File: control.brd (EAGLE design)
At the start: 100 x 20 mm, 0 parts

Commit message: adds H-bridge
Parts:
- added U$1: CHIP_PRO, CHIP_Pro-Footprint:CHIP_PRO
- added U1, U4: AL5802-7, LED Driver:SOT26
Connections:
- new net 24V: U1.2, U4.2
- new net CHG-IN: U$1.CHG-IN
- new net GND: U$1.AGND, U$1.GND@0, U$1.GND@1, U$1.GND@2, U$1.GND@3, U$1.GND@4, U$1.GND@6, U$1.GND@7, U1.4
- new net IPSOUT: U$1.IPSOUT
- new net N$1: U1.1
- new net N$2: U4.5, U4.6
- new net N$3: U1.5, U1.6
- new net N$4: U4.4
- new net N$5: U1.3
- new net N$7: U4.3
- new net N$8: U4.1
- new net VBUS: U$1.VBUS
- new net VCC3V3: U$1.VCC3V3
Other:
- board size 100 x 20 mm -> 883.9 x 101.3 mm

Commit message: adds LED driver
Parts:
- removed U1, U4: AL5802-7, LED Driver:SOT26
- added C1: UVR0J102MPD1TA, Smile_Shade:U1-M
- added C2: ESK107M025AE3EA, Smile_Shade:E-E3
- added R1, R10, R11, R12, R13, R14, R15, R16, R2, R3, R4, R5, R6, R7, R8, R9: RC0603FR-0710RL, LED Driver:RC0603N
- added U$10, U$12, U$14, U$16, U$18, U$20, U$22, U$24, U$26, U$28, U$30, U$32, U$34, U$4, U$6, U$8: 2N7002P, LED Driver:SOT23
- added U$11, U$13, U$15, U$17, U$19, U$21, U$23, U$25, U$27, U$29, U$3, U$31, U$33, U$5, U$7, U$9: NUD4011DR2G, LED Driver:8SOIC
- added U$2: L293DNE, LED Driver:NE16
- added U$35: LM2576HVT-5.0/NOPB, LED Driver:T05A
- added U$36: SRN8040-101M, Smile_Shade:IND_BOURNS_SRN8040
- moved U$1 55.0 mm to (25.4, 17.8), turned to 90 degrees
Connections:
- removed net CHG-IN: U$1.CHG-IN
- new net 48V: C2.1, R1.2, R10.2, R11.2, R12.2, R13.2, R14.2, R15.2, R16.2, R2.2, R3.2, R4.2, R5.2, R6.2, R7.2, R8.2, R9.2, U$11.P$1, U$13.P$1, U$15.P$1, U$17.P$1, U$19.P$1, U$21.P$1, U$23.P$1, U$25.P$1, U$27.P$1, U$29.P$1, U$3.P$1, U$31.P$1, U$33.P$1, U$5.P$1, U$7.P$1, U$9.P$1
- new net 5V: C1.2, U$1.CHG-IN, U$2.16, U$35.4, U$36.2
- new net AGND: U$1.AGND
- new net DIR1A: U$2.7
- new net LEDSTR_1: U$17.P$5, U$17.P$6, U$17.P$7, U$17.P$8
- new net LEDSTR_10: U$21.P$5, U$21.P$6, U$21.P$7, U$21.P$8
- new net LEDSTR_11: U$23.P$5, U$23.P$6, U$23.P$7, U$23.P$8
- new net LEDSTR_12: U$25.P$5, U$25.P$6, U$25.P$7, U$25.P$8
- new net LEDSTR_13: U$27.P$5, U$27.P$6, U$27.P$7, U$27.P$8
- new net LEDSTR_14: U$29.P$5, U$29.P$6, U$29.P$7, U$29.P$8
- new net LEDSTR_15: U$31.P$5, U$31.P$6, U$31.P$7, U$31.P$8
- new net LEDSTR_16: U$33.P$5, U$33.P$6, U$33.P$7, U$33.P$8
- new net LEDSTR_2: U$3.P$5, U$3.P$6, U$3.P$7, U$3.P$8
- new net LEDSTR_3: U$5.P$5, U$5.P$6, U$5.P$7, U$5.P$8
- new net LEDSTR_4: U$7.P$5, U$7.P$6, U$7.P$7, U$7.P$8
- new net LEDSTR_5: U$9.P$5, U$9.P$6, U$9.P$7, U$9.P$8
- new net LEDSTR_6: U$11.P$5, U$11.P$6, U$11.P$7, U$11.P$8
- new net LEDSTR_7: U$13.P$5, U$13.P$6, U$13.P$7, U$13.P$8
- new net LEDSTR_8: U$15.P$5, U$15.P$6, U$15.P$7, U$15.P$8
- new net LEDSTR_9: U$19.P$5, U$19.P$6, U$19.P$7, U$19.P$8
- new net M1B: U$2.6
- new net M2A: U$2.14
- new net N$10: R5.1, U$11.P$3
- new net N$11: U$13.P$4, U$14.P$3
- new net N$12: R6.1, U$13.P$3
- new net N$13: U$15.P$4, U$16.P$3
- new net N$14: R7.1, U$15.P$3
- new net N$15: U$17.P$4, U$18.P$3
- new net N$16: R8.1, U$17.P$3
- new net N$17: U$19.P$4, U$20.P$3
- new net N$18: R9.1, U$19.P$3
- new net N$19: U$21.P$4, U$22.P$3
- new net N$20: R10.1, U$21.P$3
- new net N$21: U$23.P$4, U$24.P$3
- new net N$22: R11.1, U$23.P$3
- new net N$23: U$25.P$4, U$26.P$3
- new net N$24: R12.1, U$25.P$3
- new net N$25: U$27.P$4, U$28.P$3
- new net N$26: R13.1, U$27.P$3
- new net N$27: U$29.P$4, U$30.P$3
- new net N$28: R14.1, U$29.P$3
- new net N$29: U$31.P$4, U$32.P$3
- new net N$30: R15.1, U$31.P$3
- new net N$31: U$33.P$4, U$34.P$3
- new net N$32: R16.1, U$33.P$3
- new net N$33: U$35.2, U$36.1
- new net N$34: C2.2, U$35.1
- new net N$6: R3.1, U$7.P$3
- new net N$9: U$11.P$4, U$12.P$3
- new net PWMLED1: U$4.P$2
- new net PWMLED10: U$22.P$2
- new net PWMLED11: U$24.P$2
- new net PWMLED12: U$26.P$2
- new net PWMLED13: U$28.P$2
- new net PWMLED14: U$30.P$2
- new net PWMLED15: U$32.P$2
- new net PWMLED16: U$34.P$2
- new net PWMLED2: U$6.P$2
- new net PWMLED3: U$8.P$2
- new net PWMLED4: U$10.P$2
- new net PWMLED5: U$12.P$2
- new net PWMLED6: U$14.P$2
- new net PWMLED7: U$16.P$2
- new net PWMLED8: U$18.P$2
- new net PWMLED9: U$20.P$2
- net 24V: now also U$2.8; no longer U1.2, U4.2
- net GND: now also C1.1, U$10.P$1, U$12.P$1, U$14.P$1, U$16.P$1, U$18.P$1, U$2.12, U$2.13, U$2.4, U$2.5, U$20.P$1, U$22.P$1, U$24.P$1, U$26.P$1, U$28.P$1, U$30.P$1, U$32.P$1, U$34.P$1, U$35.3, U$35.5, U$4.P$1, U$6.P$1, U$8.P$1; no longer U$1.AGND, U1.4
- net N$1: now also U$3.P$4, U$4.P$3; no longer U1.1
- net N$2: now also R1.1, U$3.P$3; no longer U4.5, U4.6
- net N$3: now also U$5.P$4, U$6.P$3; no longer U1.5, U1.6
- net N$4: now also R2.1, U$5.P$3; no longer U4.4
- net N$5: now also U$7.P$4, U$8.P$3; no longer U1.3
- net N$7: now also U$10.P$3, U$9.P$4; no longer U4.3
- net N$8: now also R4.1, U$9.P$3; no longer U4.1
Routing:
- net GND: track 0.00 -> 262.7 mm, vias 0 -> 4
- net 48V: track 0.00 -> 194.3 mm
- net 5V: track 0.00 -> 129.2 mm, vias 0 -> 1
- net N$33: track 0.00 -> 12.0 mm
- net N$34: track 0.00 -> 9.69 mm
- net N$19: track 0.00 -> 7.95 mm, vias 0 -> 1
- net N$25: track 0.00 -> 7.91 mm, vias 0 -> 1
- net N$15: track 0.00 -> 7.84 mm, vias 0 -> 1
- net N$11: track 0.00 -> 7.81 mm, vias 0 -> 1
- net N$21: track 0.00 -> 7.78 mm, vias 0 -> 1
- net N$5: track 0.00 -> 7.64 mm, vias 0 -> 1
- net N$13: track 0.00 -> 7.61 mm, vias 0 -> 1
- net N$23: track 0.00 -> 7.59 mm, vias 0 -> 1
- net N$31: track 0.00 -> 7.56 mm, vias 0 -> 1
- net N$3: track 0.00 -> 7.47 mm, vias 0 -> 1
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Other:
- board size 883.9 x 101.3 mm -> 172.7 x 35 mm

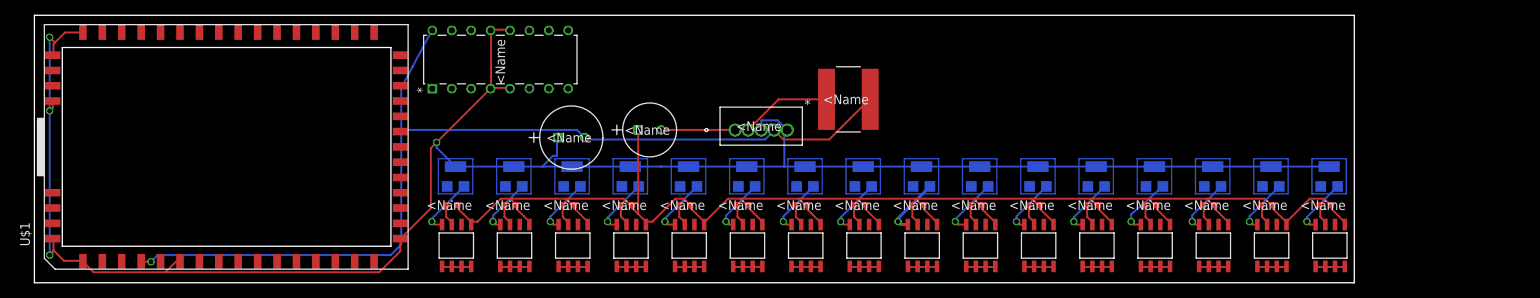
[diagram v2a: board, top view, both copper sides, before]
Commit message: adds PWM
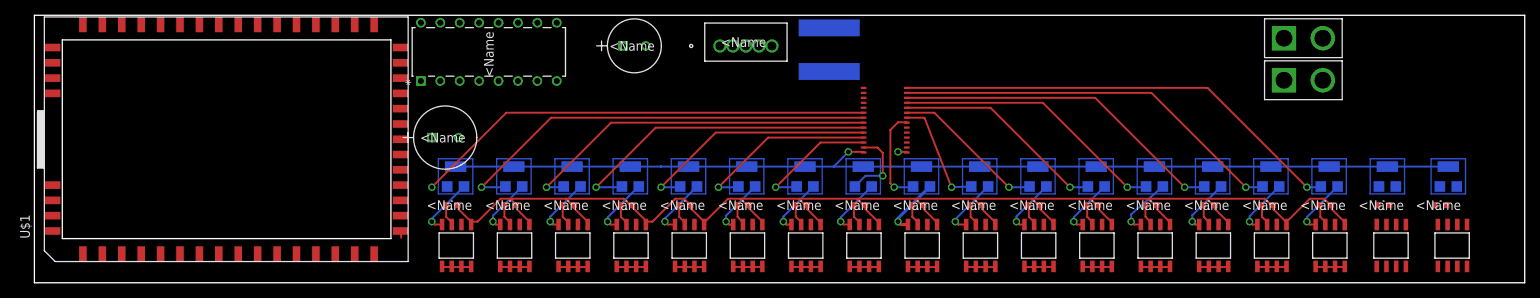
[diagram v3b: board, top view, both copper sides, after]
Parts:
- added R17, R18: RC0603FR-0710RL, LED Driver:RC0603N
- added U$37: PCA9685PW/Q900, Smile_Shade:SOT361-1
- added U$38, U$39: MOTORCONNECTOR, Smile_Shade:MOTORCONNECTOR
- added U$40, U$42: NUD4011DR2G, LED Driver:8SOIC
- added U$41, U$43: 2N7002P, LED Driver:SOT23
- moved C1 16.5 mm to (55.5, 19.0)
- moved C2 11.2 mm to (80.0, 31.0)
- moved U$35 11.2 mm to (96.5, 32.0)
- moved U$36 6.96 mm to (104.0, 30.5), flipped to the bottom, turned to 270 degrees
- moved U$2 1.80 mm to (68.3, 34.0)
- moved U$1 1.00 mm to (25.4, 18.8)
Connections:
- removed net PWMLED1: U$4.P$2
- removed net PWMLED10: U$22.P$2
- removed net PWMLED11: U$24.P$2
- removed net PWMLED12: U$26.P$2
- removed net PWMLED13: U$28.P$2
- removed net PWMLED14: U$30.P$2
- removed net PWMLED15: U$32.P$2
- removed net PWMLED16: U$34.P$2
- removed net PWMLED2: U$6.P$2
- removed net PWMLED3: U$8.P$2
- removed net PWMLED4: U$10.P$2
- removed net PWMLED5: U$12.P$2
- removed net PWMLED6: U$14.P$2
- removed net PWMLED7: U$16.P$2
- removed net PWMLED8: U$18.P$2
- removed net PWMLED9: U$20.P$2
- new net 48: R17.2, U$40.P$1
- new net LEDSTR_17: U$40.P$5, U$40.P$6, U$40.P$7, U$40.P$8
- new net LEDSTR_18: U$42.P$5, U$42.P$6, U$42.P$7, U$42.P$8
- new net M0: U$1.PWM0, U$2.1
- new net M1: U$1.PWM1, U$2.9
- new net M1A: U$2.3, U$38.P$2
- new net M2B: U$2.11, U$39.P$2
- new net N$35: U$40.P$4, U$41.P$3
- new net N$36: R17.1, U$40.P$3
- new net N$37: U$42.P$4, U$43.P$3
- new net N$38: R18.1, U$42.P$3
- new net SCK: U$1.TWI1-SCK, U$37.P$26
- new net SDA: U$1.TWI1-SDA, U$37.P$27
- new net ZN0: U$18.P$2, U$37.P$6
- new net ZN1: U$37.P$7, U$4.P$2
- new net ZN10: U$30.P$2, U$37.P$17
- new net ZN11: U$28.P$2, U$37.P$18
- new net ZN12: U$26.P$2, U$37.P$19
- new net ZN13: U$20.P$2, U$37.P$20
- new net ZN14: U$22.P$2, U$37.P$21
- new net ZN15: U$24.P$2, U$37.P$22
- new net ZN16: U$43.P$2
- new net ZN2: U$37.P$8, U$6.P$2
- new net ZN3: U$37.P$9, U$8.P$2
- new net ZN4: U$14.P$2, U$37.P$10
- new net ZN5: U$12.P$2, U$37.P$11
- new net ZN6: U$10.P$2, U$37.P$12
- new net ZN7: U$16.P$2, U$37.P$13
- new net ZN8: U$34.P$2, U$37.P$15, U$41.P$2
- new net ZN9: U$32.P$2, U$37.P$16
- net 48V: now also R18.2, U$42.P$1
- net 5V: now also U$37.P$28
- net GND: now also U$37.P$14, U$41.P$1, U$43.P$1
- net M1B: now also U$38.P$1
- net M2A: now also U$39.P$1
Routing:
- net 5V: track 129.2 -> 1.20 mm
- net GND: track 262.7 -> 135.7 mm, vias 4 -> 1
- net ZN0: track 0.00 -> 60.7 mm, vias 0 -> 1
- net ZN8: track 0.00 -> 59.6 mm, vias 0 -> 1
- net ZN1: track 0.00 -> 56.9 mm, vias 0 -> 1
- net ZN9: track 0.00 -> 51.7 mm, vias 0 -> 1
- net ZN2: track 0.00 -> 47.3 mm, vias 0 -> 1
- net ZN10: track 0.00 -> 43.8 mm, vias 0 -> 1
- net ZN3: track 0.00 -> 41.6 mm, vias 0 -> 1
- net ZN11: track 0.00 -> 35.9 mm, vias 0 -> 1
- net ZN4: track 0.00 -> 32.0 mm, vias 0 -> 1
- net ZN12: track 0.00 -> 28.0 mm, vias 0 -> 1
- net ZN5: track 0.00 -> 24.3 mm, vias 0 -> 1
- net ZN13: track 0.00 -> 20.1 mm, vias 0 -> 1
- net ZN6: track 0.00 -> 16.7 mm, vias 0 -> 1
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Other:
- board size 172.7 x 35 mm -> 195 x 35 mm

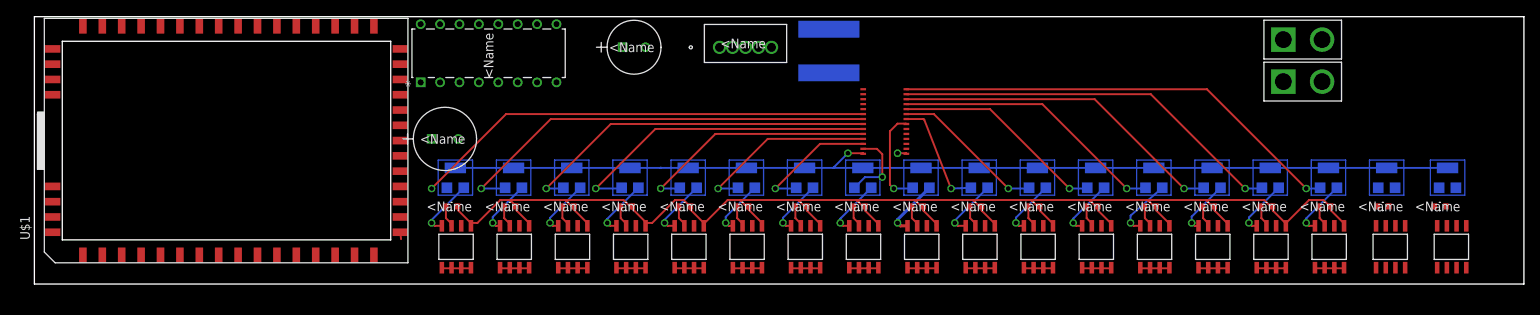
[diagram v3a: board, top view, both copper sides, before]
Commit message: adds flex connector
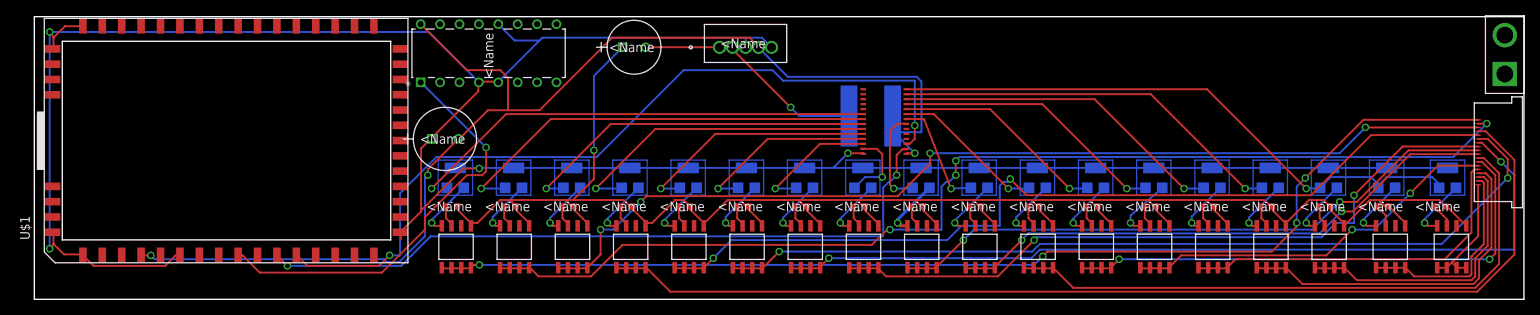
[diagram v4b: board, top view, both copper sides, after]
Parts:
- U$39: value MOTORCONNECTOR -> SFV18R-3STBE1HLF; device Smile_Shade:MOTORCONNECTOR -> Smile_Shade:SFV18R-3STBE1HLF
- moved U$39 31.8 mm to (189.0, 13.0), turned to 90 degrees
- moved U$38 29.0 mm to (192.5, 27.5), turned to 90 degrees
- moved U$36 10.1 mm to (109.5, 22.0), turned to 180 degrees
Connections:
- net LEDSTR_1: now also U$39.P$18
- net LEDSTR_10: now also U$39.P$9
- net LEDSTR_11: now also U$39.P$10
- net LEDSTR_12: now also U$39.P$7
- net LEDSTR_13: now also U$39.P$6
- net LEDSTR_14: now also U$39.P$5
- net LEDSTR_15: now also U$39.P$4
- net LEDSTR_16: now also U$39.P$3
- net LEDSTR_17: now also U$39.P$1
- net LEDSTR_18: now also U$39.P$2
- net LEDSTR_2: now also U$39.P$17
- net LEDSTR_3: now also U$39.P$16
- net LEDSTR_4: now also U$39.P$15
- net LEDSTR_5: now also U$39.P$12
- net LEDSTR_6: now also U$39.P$13
- net LEDSTR_7: now also U$39.P$14
- net LEDSTR_8: now also U$39.P$11
- net LEDSTR_9: now also U$39.P$8
- net M1A: no longer U$38.P$2
- net M1B: no longer U$38.P$1
- net M2A: now also U$38.P$1; no longer U$39.P$1
- net M2B: now also U$38.P$2; no longer U$39.P$2
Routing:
- net GND: track 135.7 -> 333.7 mm, vias 1 -> 4
- net 5V: track 1.20 -> 160.3 mm, vias 1 -> 3
- net LEDSTR_1: track 4.04 -> 147.0 mm, vias 0 -> 4
- net LEDSTR_2: track 3.97 -> 143.6 mm, vias 0 -> 4
- net LEDSTR_4: track 4.01 -> 139.7 mm
- net LEDSTR_3: track 4.03 -> 131.0 mm, vias 0 -> 4
- net LEDSTR_7: track 4.03 -> 117.4 mm, vias 0 -> 2
- net LEDSTR_6: track 3.97 -> 113.9 mm, vias 0 -> 2
- net LEDSTR_5: track 4.04 -> 112.2 mm, vias 0 -> 2
- net SCK: track 0.00 -> 106.5 mm, vias 0 -> 2
- net SDA: track 0.00 -> 94.6 mm, vias 0 -> 2
- net LEDSTR_8: track 4.02 -> 92.2 mm, vias 0 -> 2
- net LEDSTR_11: track 4.02 -> 81.3 mm, vias 0 -> 2
- net LEDSTR_9: track 3.97 -> 80.2 mm
- net LEDSTR_10: track 4.04 -> 73.5 mm, vias 0 -> 2
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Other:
- board size 195 x 35 mm -> 195 x 37 mm

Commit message: Revert "adds flex connector"
This reverts commit c0465f8f5036756819879aef16fe9e16a98b933a.
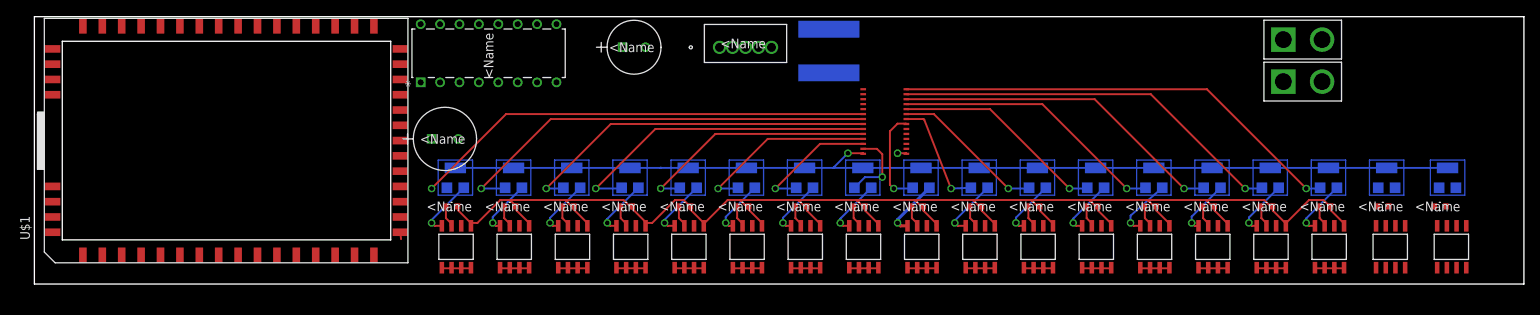
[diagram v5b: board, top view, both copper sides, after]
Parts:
- U$39: value SFV18R-3STBE1HLF -> MOTORCONNECTOR; device Smile_Shade:SFV18R-3STBE1HLF -> Smile_Shade:MOTORCONNECTOR
- moved U$39 31.8 mm to (163.5, 32.0), turned to 0 degrees
- moved U$38 29.0 mm to (163.5, 26.5), turned to 0 degrees
- moved U$36 10.1 mm to (104.0, 30.5), turned to 270 degrees
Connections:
- net LEDSTR_1: no longer U$39.P$18
- net LEDSTR_10: no longer U$39.P$9
- net LEDSTR_11: no longer U$39.P$10
- net LEDSTR_12: no longer U$39.P$7
- net LEDSTR_13: no longer U$39.P$6
- net LEDSTR_14: no longer U$39.P$5
- net LEDSTR_15: no longer U$39.P$4
- net LEDSTR_16: no longer U$39.P$3
- net LEDSTR_17: no longer U$39.P$1
- net LEDSTR_18: no longer U$39.P$2
- net LEDSTR_2: no longer U$39.P$17
- net LEDSTR_3: no longer U$39.P$16
- net LEDSTR_4: no longer U$39.P$15
- net LEDSTR_5: no longer U$39.P$12
- net LEDSTR_6: no longer U$39.P$13
- net LEDSTR_7: no longer U$39.P$14
- net LEDSTR_8: no longer U$39.P$11
- net LEDSTR_9: no longer U$39.P$8
- net M1A: now also U$38.P$2
- net M1B: now also U$38.P$1
- net M2A: now also U$39.P$1; no longer U$38.P$1
- net M2B: now also U$39.P$2; no longer U$38.P$2
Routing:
- net GND: track 333.7 -> 135.7 mm, vias 4 -> 1
- net 5V: track 160.3 -> 1.20 mm, vias 3 -> 1
- net LEDSTR_1: track 147.0 -> 4.04 mm, vias 4 -> 0
- net LEDSTR_2: track 143.6 -> 3.97 mm, vias 4 -> 0
- net LEDSTR_4: track 139.7 -> 4.01 mm
- net LEDSTR_3: track 131.0 -> 4.03 mm, vias 4 -> 0
- net LEDSTR_7: track 117.4 -> 4.03 mm, vias 2 -> 0
- net LEDSTR_6: track 113.9 -> 3.97 mm, vias 2 -> 0
- net LEDSTR_5: track 112.2 -> 4.04 mm, vias 2 -> 0
- net SCK: track 106.5 -> 0.00 mm, vias 2 -> 0
- net SDA: track 94.6 -> 0.00 mm, vias 2 -> 0
- net LEDSTR_8: track 92.2 -> 4.02 mm, vias 2 -> 0
- net LEDSTR_11: track 81.3 -> 4.02 mm, vias 2 -> 0
- net LEDSTR_9: track 80.2 -> 3.97 mm
- net LEDSTR_10: track 73.5 -> 4.04 mm, vias 2 -> 0
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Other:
- board size 195 x 37 mm -> 195 x 35 mm
